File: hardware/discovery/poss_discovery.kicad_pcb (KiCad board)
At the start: 2 copper layers, 96.5 x 66 mm, 84 parts, among them CON1 USB-MICRO-B, SW1 SW_PUSH, SW10 SW_PUSH, SW11 SW_PUSH, SW12 SW_PUSH, SW13 SW_PUSH, SW14 SW_PUSH, SW15 SW_PUSH, SW16 SW_PUSH, SW17 SW_PUSH, SW18 SW_PUSH, SW19 SW_PUSH, SW2 SW_PUSH, SW20 SW_PUSH, SW21 SW_PUSH, SW22 SW_PUSH, SW3 SW_PUSH, SW4 SW_PUSH, SW5 SW_PUSH, SW6 SW_PUSH, SW7 SW_PUSH, SW8 SW_PUSH, SW9 SW_PUSH, U2 MCP73831, U3 BD33IA5, U4 STM32F407VG, U5 SGTL5000, X1 CRYSTAL

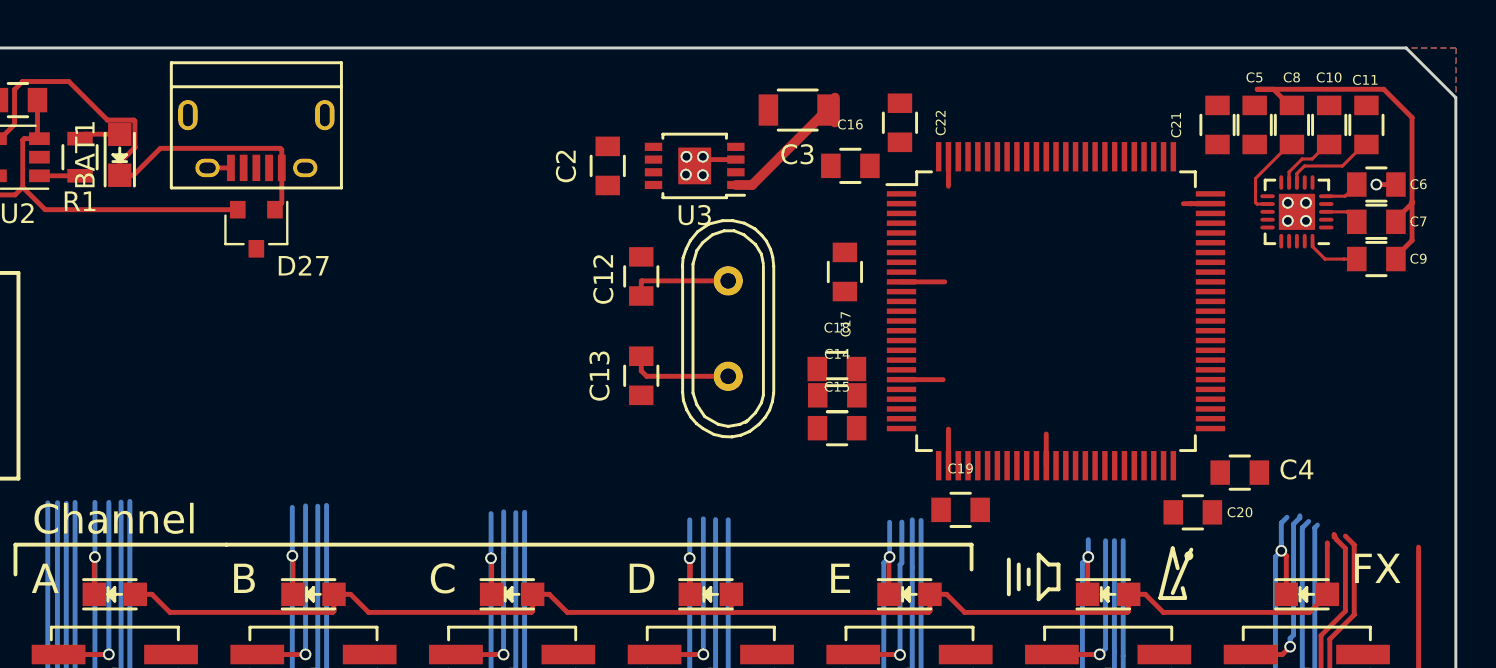
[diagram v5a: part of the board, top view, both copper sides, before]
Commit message: Discovery: Fix pull-ups and add LED current limiters
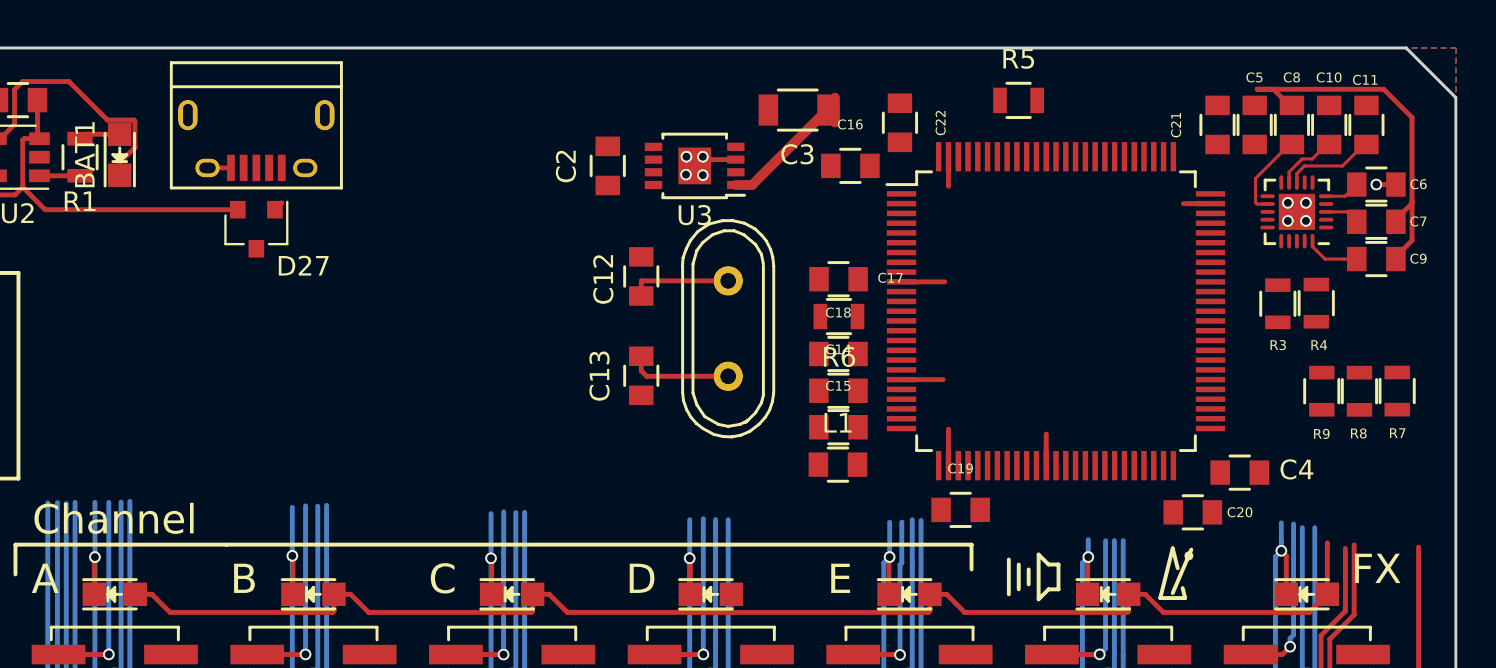
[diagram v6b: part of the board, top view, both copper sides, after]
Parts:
- added L1: 15Ohm, Capacitors_SMD:C_0805, F.Cu at (144.9, 100.0)
- added R3: 10K, Resistors_SMD:R_0805, F.Cu at (167.4, 91.8)
- added R4: 10K, Resistors_SMD:R_0805, F.Cu at (169.4, 91.8)
- added R5: 10K, Resistors_SMD:R_0805, F.Cu at (154.2, 81.4)
- added R6: 10K, Resistors_SMD:R_0805, F.Cu at (145.0, 92.5)
- added R7: R, Resistors_SMD:R_0805, F.Cu at (173.5, 96.3)
- added R8: R, Resistors_SMD:R_0805, F.Cu at (171.6, 96.3)
- added R9: R, Resistors_SMD:R_0805, F.Cu at (169.7, 96.3)
- moved C18 0.77 mm to (145.0, 94.4)
- moved C17 0.49 mm to (145.0, 90.6), turned to 0 degrees
- moved C14 0.24 mm to (145.0, 96.3)
- moved C15 0.08 mm to (145.0, 98.1)
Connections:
- net ROW1 renamed Net-(D1-Pad2)
- net ROW2 renamed Net-(D10-Pad2)
- net ROW3 renamed Net-(D19-Pad2)
- CON1 pad 1: VBUS -> Net-(CON1-Pad1)
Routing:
- net VBUS: track 25.9 -> 13.8 mm
- net Net-(D10-Pad2): track 106.9 -> 105.8 mm
- net Net-(D1-Pad2): track 118.6 -> 118.0 mm
- net FX: track 9.09 -> 8.53 mm

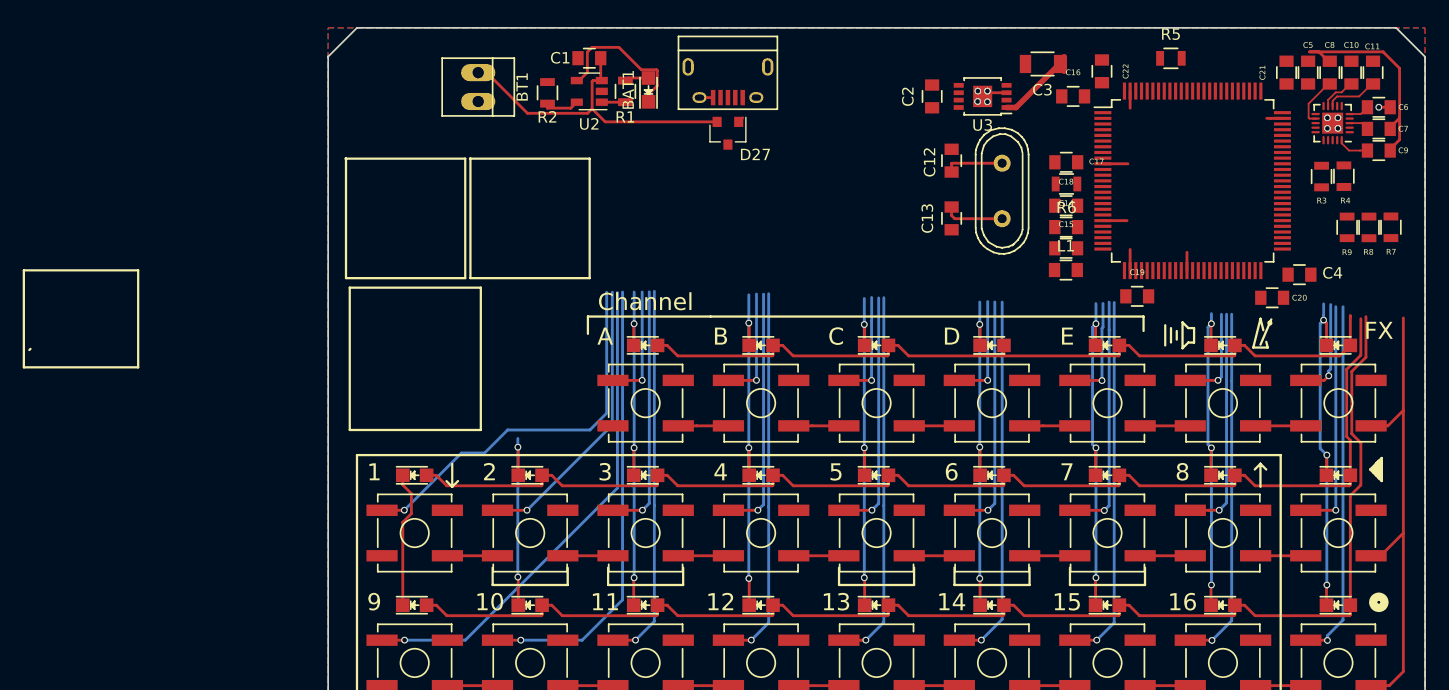
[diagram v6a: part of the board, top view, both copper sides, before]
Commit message: Discovery: Start routing LEDs and buttons
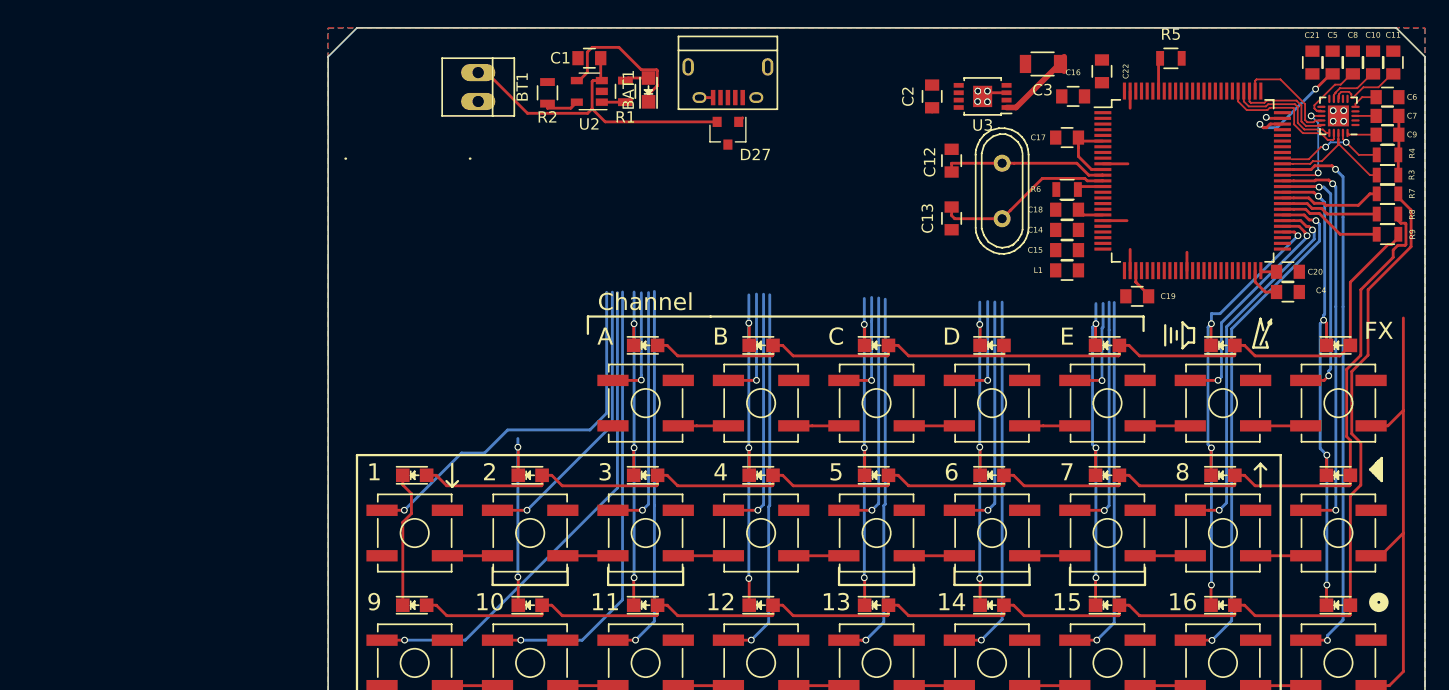
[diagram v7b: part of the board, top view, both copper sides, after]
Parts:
- moved R3 5.80 mm to (173.2, 91.7), turned to 180 degrees
- moved R4 4.27 mm to (173.2, 89.9), turned to 180 degrees
- moved R9 3.60 mm to (173.2, 96.9), turned to 0 degrees
- moved R7 2.96 mm to (173.2, 93.3), turned to 0 degrees
- moved C20 2.67 mm to (164.5, 100.2)
- moved C21 2.45 mm to (166.6, 81.8)
- moved C5 2.33 mm to (168.4, 81.8)
- moved C8 2.22 mm to (170.2, 81.8)
- moved C17 2.18 mm to (145.0, 88.4)
- moved C10 2.10 mm to (172.0, 81.8)
- moved R8 2.00 mm to (173.2, 95.1), turned to 0 degrees
- moved C11 1.99 mm to (173.7, 81.8)
- moved C4 1.83 mm to (164.5, 102.0)
- moved C9 1.59 mm to (173.2, 88.1)
- moved C7 1.37 mm to (173.2, 86.5)
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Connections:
- U4 pad 29: I2S_LRCLK -> Net-(U4-Pad29)
- U4 pad 54: Net-(U4-Pad54) -> COL8
- U4 pad 55: Net-(U4-Pad55) -> BPM_VOL
- U4 pad 56: Net-(U4-Pad56) -> B8
- U4 pad 57: Net-(U4-Pad57) -> B16
- U4 pad 58: Net-(U4-Pad58) -> ROW3
- U4 pad 59: Net-(U4-Pad59) -> ROW2
- U4 pad 60: Net-(U4-Pad60) -> ROW1
- U4 pad 61: Net-(U4-Pad61) -> COL9
- U4 pad 62: Net-(U4-Pad62) -> FX
- U4 pad 63: Net-(U4-Pad63) -> Play
- U4 pad 65: Net-(U4-Pad65) -> Write
- U4 pad 66: Net-(U4-Pad66) -> Audio_SDA
- U4 pad 67: Net-(U4-Pad67) -> Audio_SCL
- U4 pad 77: Net-(U4-Pad77) -> I2S_LRCLK
- U4 pad 92: Audio_SCL -> Net-(U4-Pad92)
- U4 pad 96: Audio_SDA -> Net-(U4-Pad96)
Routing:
- net Write: track 31.8 -> 49.1 mm, vias 1 -> 2
- net Play: track 20.6 -> 36.1 mm, vias 1 -> 2
- net B16: track 31.3 -> 46.1 mm, vias 1 -> 2
- net FX: track 8.53 -> 22.8 mm, vias 1 -> 2
- net B8: track 20.1 -> 33.7 mm, vias 1 -> 2
- net COL9: track 31.0 -> 44.1 mm, vias 3 -> 4
- net Net-(D1-Pad2): track 118.0 -> 130.9 mm
- net BPM_VOL: track 8.38 -> 21.0 mm, vias 1 -> 2
- net I2S_DIN: track 0.00 -> 12.3 mm
- net COL8: track 30.3 -> 42.2 mm, vias 3 -> 4
- net Net-(D10-Pad2): track 105.8 -> 117.6 mm
- net Audio_SDA: track 0.00 -> 11.6 mm
- net Net-(C5-Pad1): track 0.00 -> 10.7 mm, vias 0 -> 2
- net I2S_DOUT: track 0.00 -> 10.6 mm
- net Net-(C13-Pad2): track 5.31 -> 15.8 mm
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
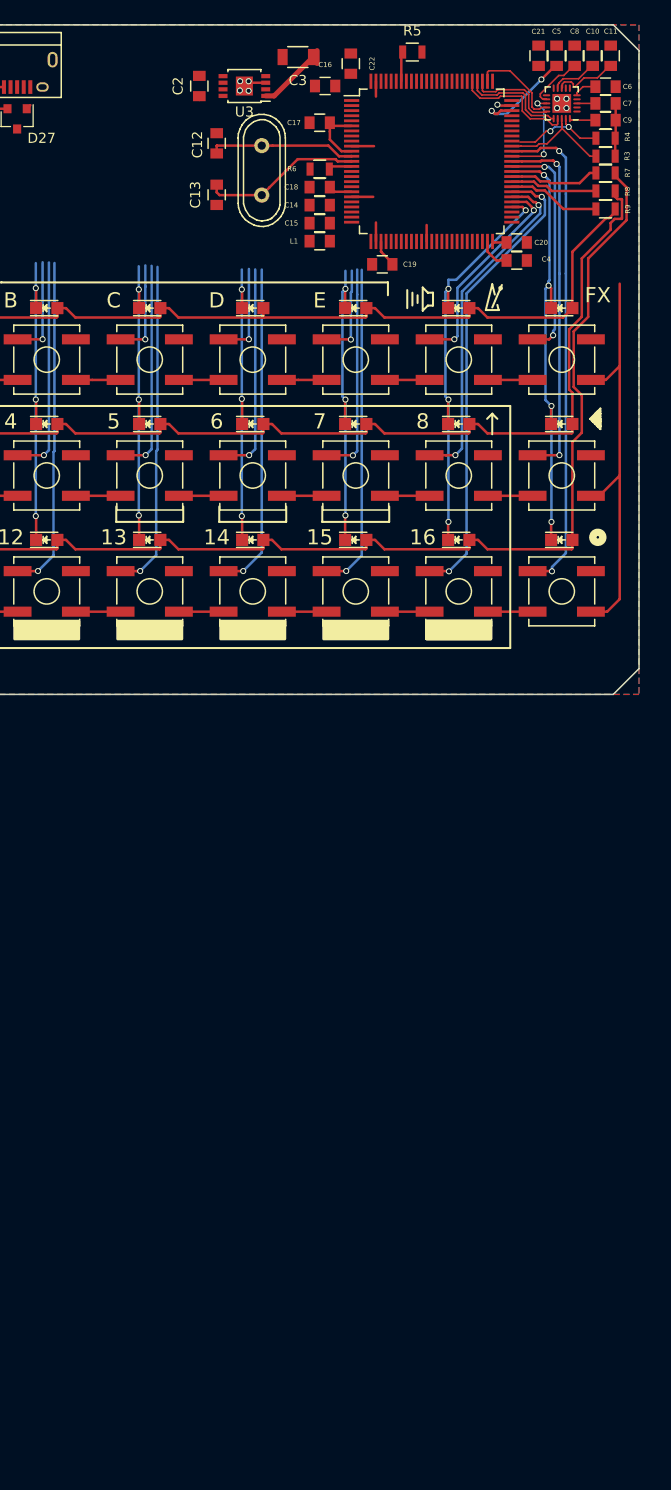
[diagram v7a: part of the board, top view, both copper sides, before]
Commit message: Discovery LEDs and button routing part 2
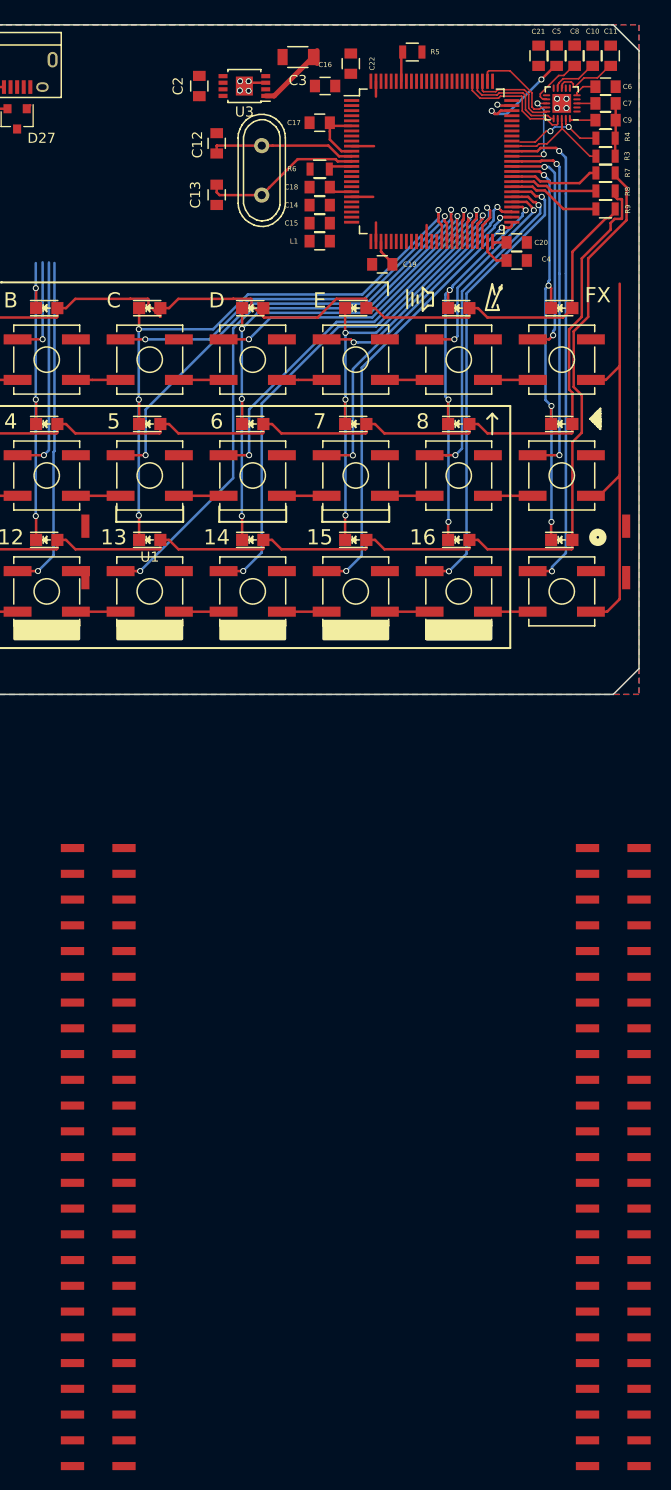
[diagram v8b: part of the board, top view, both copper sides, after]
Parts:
- added U1: STM32F4_DISCO_Header, stm32f4-disco:STM32F4-DISCO-HEADERS-SMD, F.Cu at (128.3, 154.9)
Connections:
- net SPI1_MISO renamed Net-(U4-Pad31)
- net SPI1_MOSI renamed Net-(U4-Pad32)
- net SPI1_SCK renamed Net-(U4-Pad30)
- U4 pad 40: Net-(U4-Pad40) -> COL5
- U4 pad 41: Net-(U4-Pad41) -> BC
- U4 pad 42: Net-(U4-Pad42) -> B5
- U4 pad 43: Net-(U4-Pad43) -> B13
- U4 pad 44: Net-(U4-Pad44) -> COL6
- U4 pad 45: Net-(U4-Pad45) -> BD
- U4 pad 46: Net-(U4-Pad46) -> B6
- U4 pad 47: Net-(U4-Pad47) -> B14
- U4 pad 48: Net-(U4-Pad48) -> COL7
- U4 pad 51: Net-(U4-Pad51) -> B15
- U4 pad 52: Net-(U4-Pad52) -> B7
- U4 pad 53: Net-(U4-Pad53) -> BE
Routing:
- net COL5: track 31.3 -> 63.5 mm, vias 3 -> 4
- net BC: track 9.74 -> 39.7 mm, vias 1 -> 2
- net B5: track 21.4 -> 49.0 mm, vias 1 -> 2
- net B13: track 32.6 -> 59.1 mm, vias 1 -> 2
- net COL6: track 31.0 -> 55.8 mm, vias 3 -> 4
- net BD: track 9.43 -> 32.3 mm, vias 1 -> 2
- net B6: track 21.1 -> 41.4 mm, vias 1 -> 2
- net B14: track 32.4 -> 51.8 mm, vias 1 -> 2
- net COL7: track 31.2 -> 49.2 mm, vias 3 -> 4
- net BE: track 9.23 -> 24.8 mm, vias 1 -> 2
- net B7: track 21.1 -> 33.2 mm, vias 1 -> 2
- net B15: track 32.3 -> 43.6 mm, vias 1 -> 2
- net Net-(D19-Pad2): track 79.4 -> 82.2 mm
- net COL8: track 42.2 -> 41.7 mm
